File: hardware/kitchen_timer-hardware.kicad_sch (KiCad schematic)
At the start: 20 parts, among them J1 AVR-ISP-6, SW1 SW_Push_Open_Dual, U1 ATmega328P-A, U2 BMS Module, U3 UART_Module, U4 AP2111H-3.3, Y1 Crystal

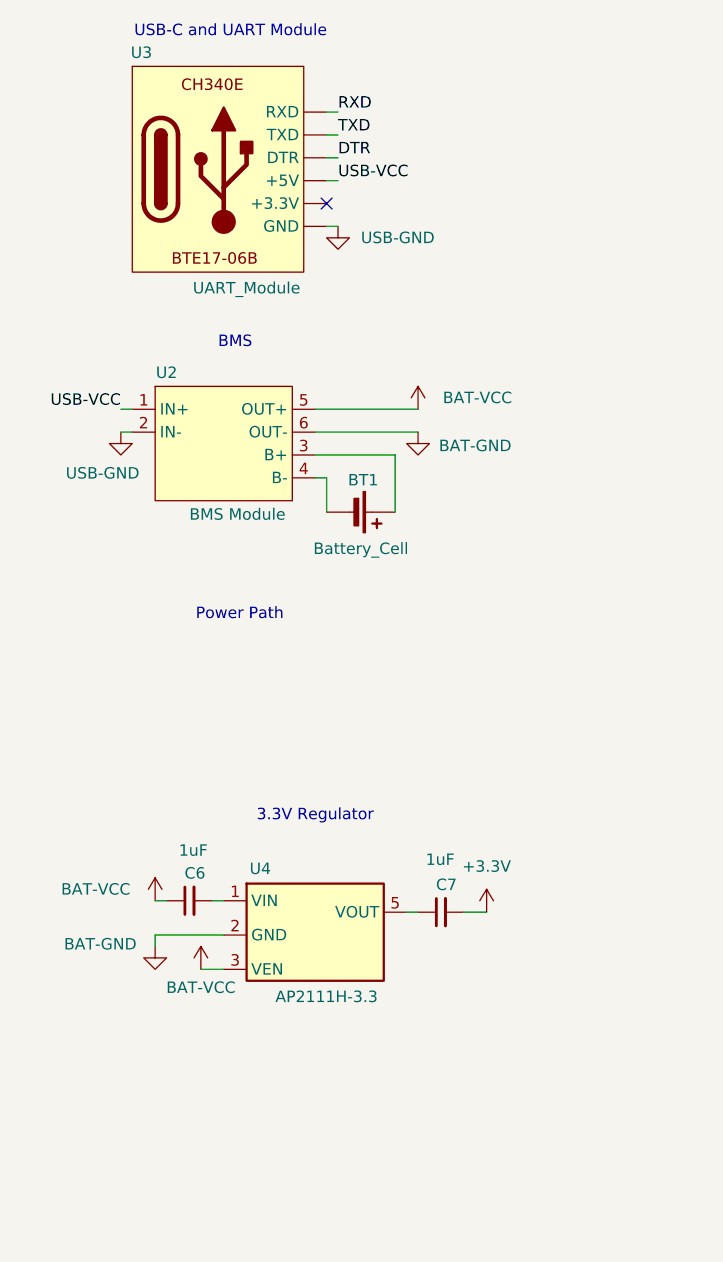
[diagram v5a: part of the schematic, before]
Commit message: Added Power Path schematic
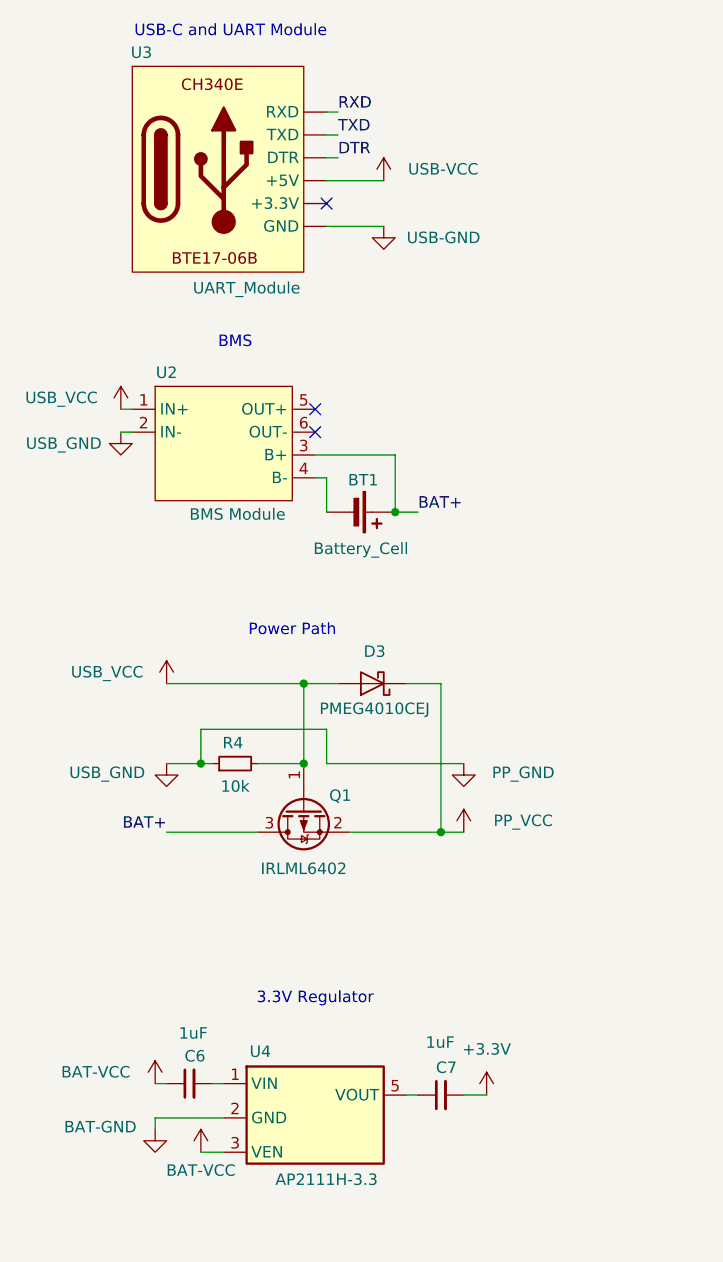
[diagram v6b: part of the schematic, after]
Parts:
- added D3: PMEG4010CEJ, Diode_SMD:D_SOD-323F, symbol Diode:PMEG4010CEJ
- added Q1: IRLML6402, Package_TO_SOT_SMD:SOT-23, symbol Transistor_FET:IRLML6402
- added R4: 10k, symbol Device:R_Small
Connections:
- net BAT-GND: no longer U2.6 (OUT-)
- net BAT-VCC: no longer U2.5 (OUT+)
- net USB-GND: no longer U2.2 (IN-)
- net USB-VCC: no longer U2.1 (IN+)
- net BAT+: now reaches BT1.1 (+), U2.3 (B+)
- net BAT+: now also Q1.3 (D)
- new net PP_GND: R4.1, U2.2 (IN-)
- new net PP_VCC: D3.1 (K), Q1.2 (S)
- new net USB_VCC: D3.2 (A), Q1.1 (G), R4.2, U2.1 (IN+)
- no-connect marks 1 -> 3
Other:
- moved on the sheet: C6, C7, U4

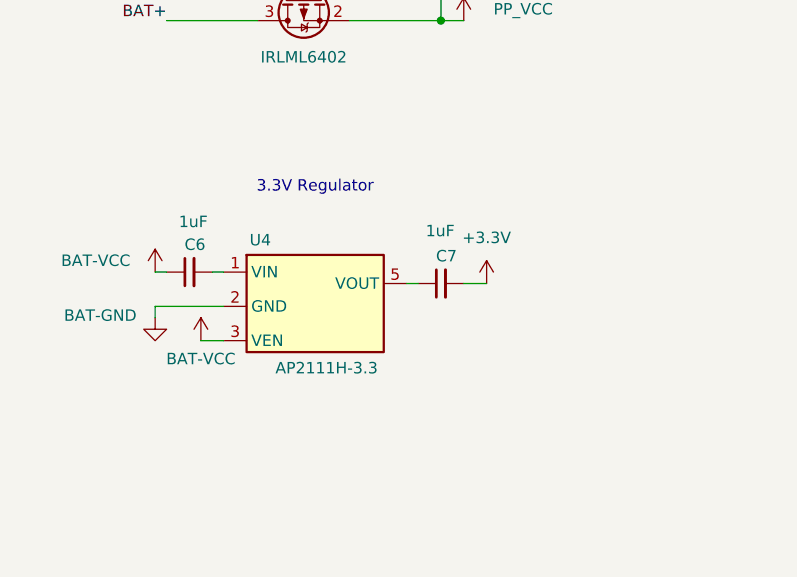
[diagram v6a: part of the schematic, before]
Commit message: Updated 3.3V Regulator as per the schematic on the Datasheet.
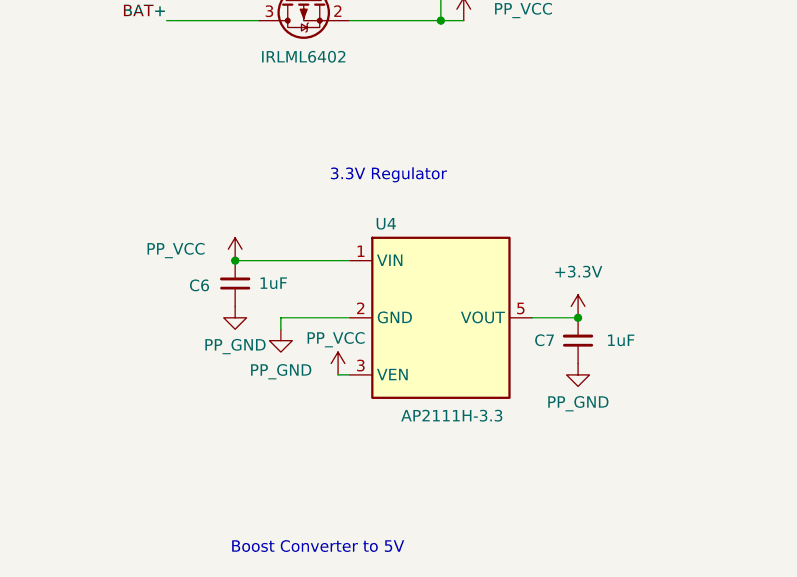
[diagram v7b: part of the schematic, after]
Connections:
- net BAT-GND is gone; now on net PP_GND: U4.2 (GND)
- net +3.3V: now also U4.5 (VOUT)
- net PP_GND: now also C6.1, C7.1
- net PP_VCC: now also C6.2, U4.1 (VIN), U4.3 (VEN)
- removed net BAT-VCC: C6.1, U4.3 (VEN)
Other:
- note added: "Boost Converter to 5V"
- moved on the sheet: U4

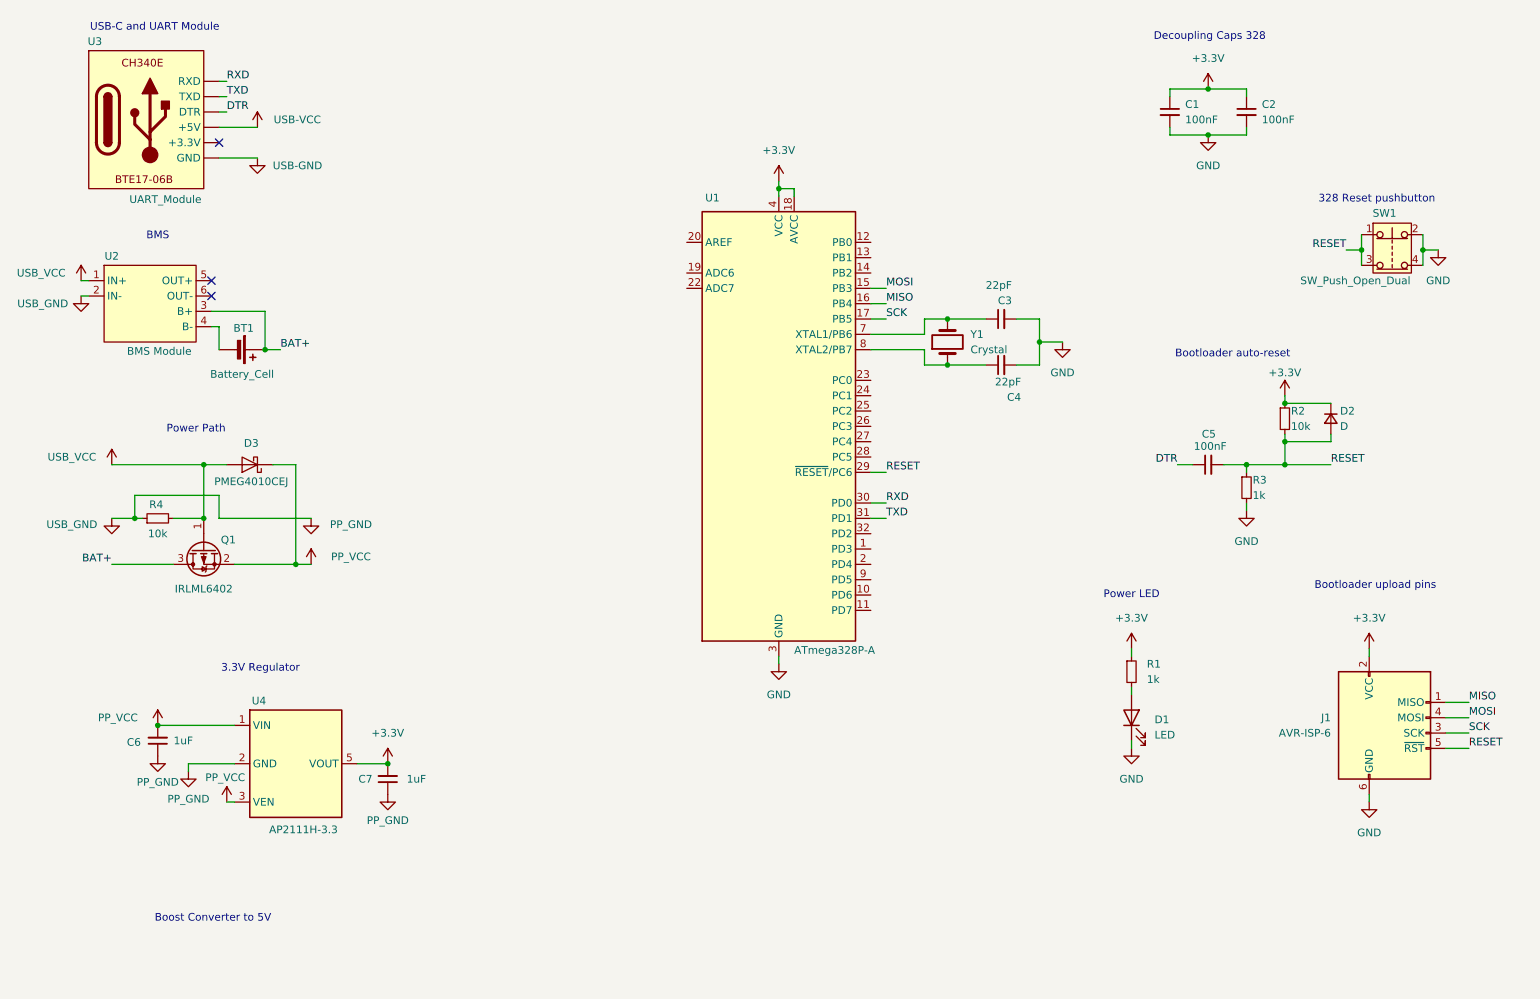
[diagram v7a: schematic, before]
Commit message: Added the 5V Boost Converter
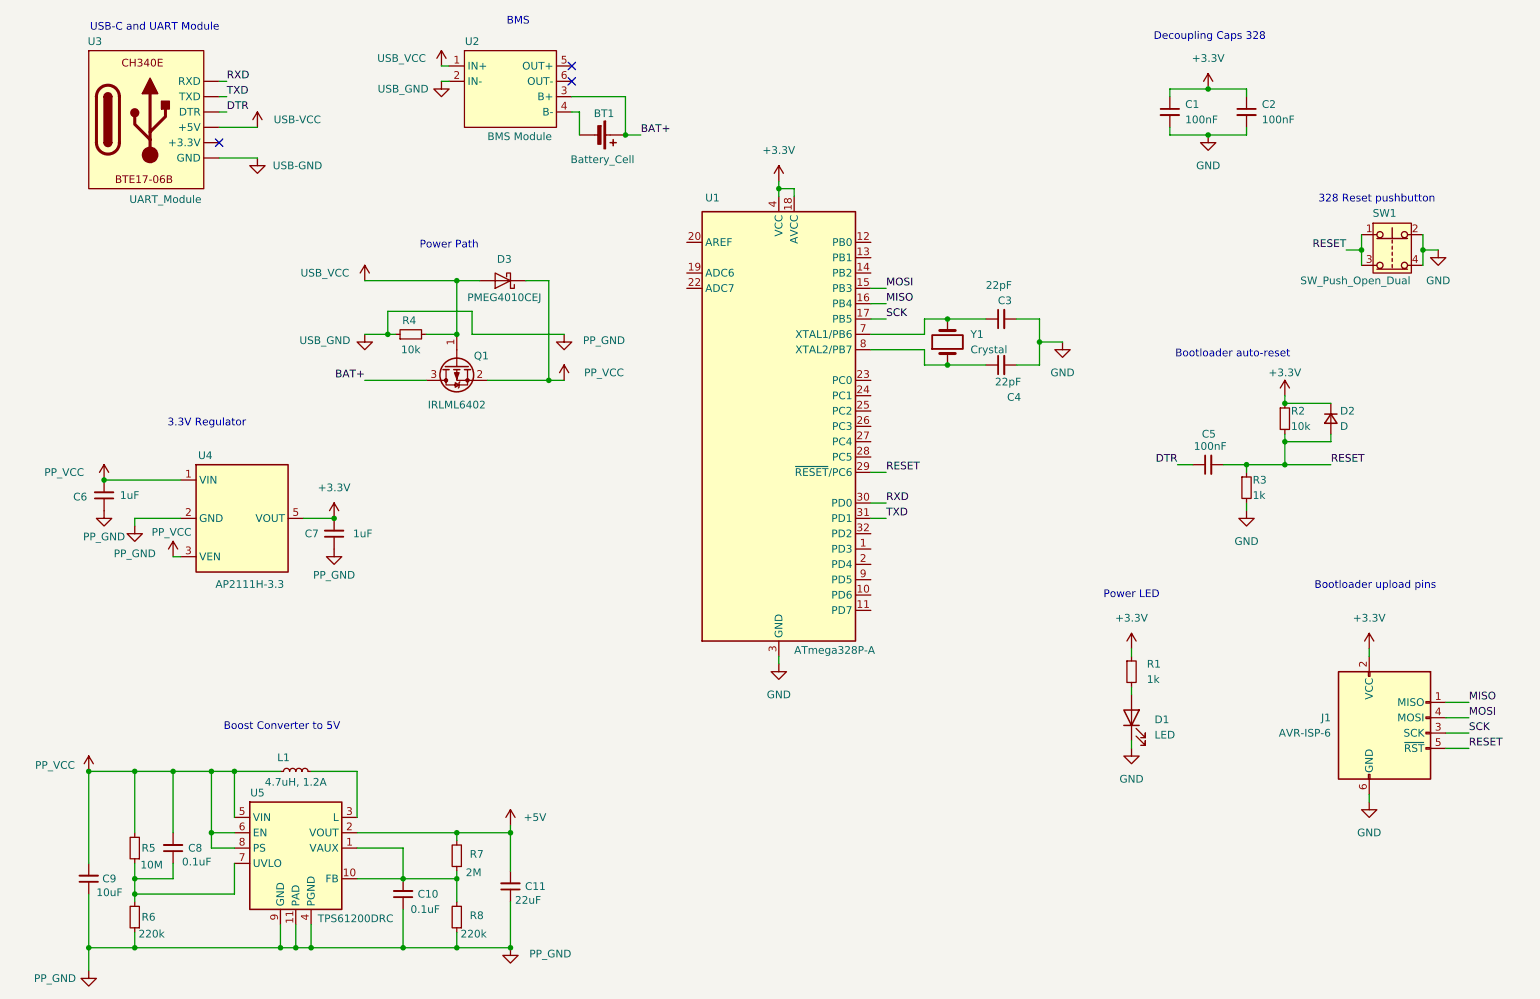
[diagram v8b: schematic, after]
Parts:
- added C10, C8: 0.1uF, symbol Device:C_Small
- added C11: 22uF, symbol Device:C_Small
- added C9: 10uF, symbol Device:C_Small
- added L1: 4.7uH, 1.2A, symbol Device:L_Small
- added R5: 10M, symbol Device:R_Small
- added R6, R8: 220k, symbol Device:R_Small
- added R7: 2M, symbol Device:R_Small
- added U5: TPS61200DRC, Package_SON:Texas_S-PVSON-N10_ThermalVias, symbol Regulator_Switching:TPS61200DRC
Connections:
- net PP_GND: now also C10.1, C11.1, C9.1, R6.1, R8.1, U5.11 (PAD), U5.4 (PGND), U5.9 (GND)
- net PP_VCC: now also C8.2, C9.2, L1.1, R5.2, U5.5 (VIN), U5.6 (EN), U5.8 (PS)
- new net: C10.2, R7.1, R8.2, U5.1 (VAUX), U5.10 (FB)
- new net: L1.2, U5.3 (L)
- new net: C8.1, R5.1, R6.2, U5.7 (UVLO)
- new net +5V: C11.2, R7.2, U5.2 (VOUT)
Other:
- moved on the sheet: BT1, C6, C7, D3, Q1, R4, U2, U4
